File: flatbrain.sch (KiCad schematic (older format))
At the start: 101 parts, among them J1 OLED, SW1 SW_Push, U1 kbd_ProMicro

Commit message: Update mx footprints
TODO
 * verify the diode placement
 * replace right 1.75u with 1u + encoder
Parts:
- MX1, MX10, MX11, MX12, MX13, MX14, MX15, MX16, MX17, MX18, MX19, MX2, MX20, MX21, MX22, MX23, MX24, MX25, MX26, MX27, MX28, MX29, MX3, MX30, MX31, MX32, MX33, MX34, MX35, MX36, MX37, MX38, MX4, MX43, MX44, MX5, MX6, MX7, MX8, MX9: footprint MX_Only:MXOnly-1U-NoLED -> parts:mx_1u
- MX39, MX42: footprint MX_Only:MXOnly-1.75U-NoLED -> parts:mx_175u
- MX40, MX41: footprint MX_Only:MXOnly-1.5U-NoLED -> parts:mx_15u

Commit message: Correct leds connection
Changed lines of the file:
@@
 L power:GND #PWR0107
 U 1 1 5EAF3A6B
-P 1300 4650
-F 0 "#PWR0107" H 1300 4400 50  0001 C CNN
-F 1 "GND" H 1305 4477 50  0000 C CNN
-F 2 "" H 1300 4650 50  0001 C CNN
-F 3 "" H 1300 4650 50  0001 C CNN
-	1    1300 4650
-	-1   0    0    1
+P 1300 5250
+F 0 "#PWR0107" H 1300 5000 50  0001 C CNN
+F 1 "GND" H 1305 5077 50  0000 C CNN
+F 2 "" H 1300 5250 50  0001 C CNN
+F 3 "" H 1300 5250 50  0001 C CNN
+	1    1300 5250
+	1    0    0    -1
 $EndComp
 Connection ~ 1300 4650
@@
 L power:VCC #PWR0108
 U 1 1 5EAF44CC
-P 1300 5250
-F 0 "#PWR0108" H 1300 5100 50  0001 C CNN
-F 1 "VCC" H 1315 5423 50  0000 C CNN
-F 2 "" H 1300 5250 50  0001 C CNN
-F 3 "" H 1300 5250 50  0001 C CNN
-	1    1300 5250
-	-1   0    0    1
+P 1300 4650
+F 0 "#PWR0108" H 1300 4500 50  0001 C CNN
+F 1 "VCC" H 1315 4823 50  0000 C CNN
+F 2 "" H 1300 4650 50  0001 C CNN
+F 3 "" H 1300 4650 50  0001 C CNN
+	1    1300 4650
+	1    0    0    -1
 $EndComp
 Connection ~ 1300 5250

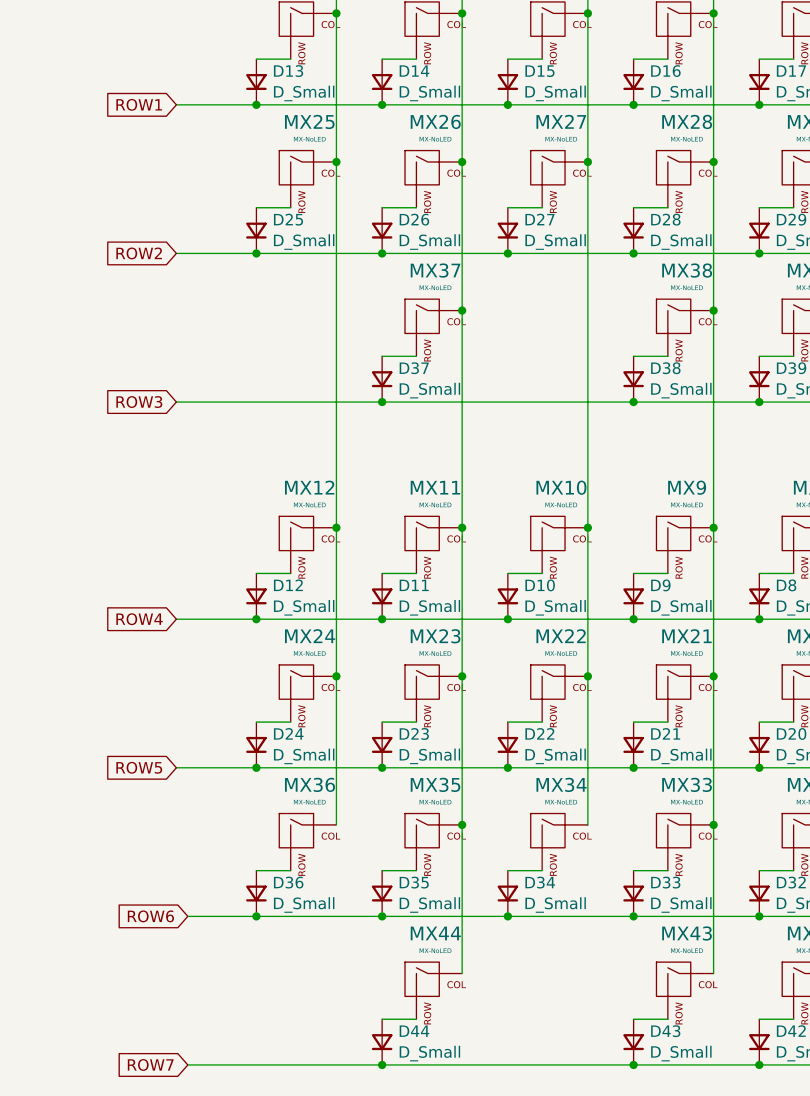
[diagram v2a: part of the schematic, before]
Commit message: Move lowest pinky keys to thumb cluster
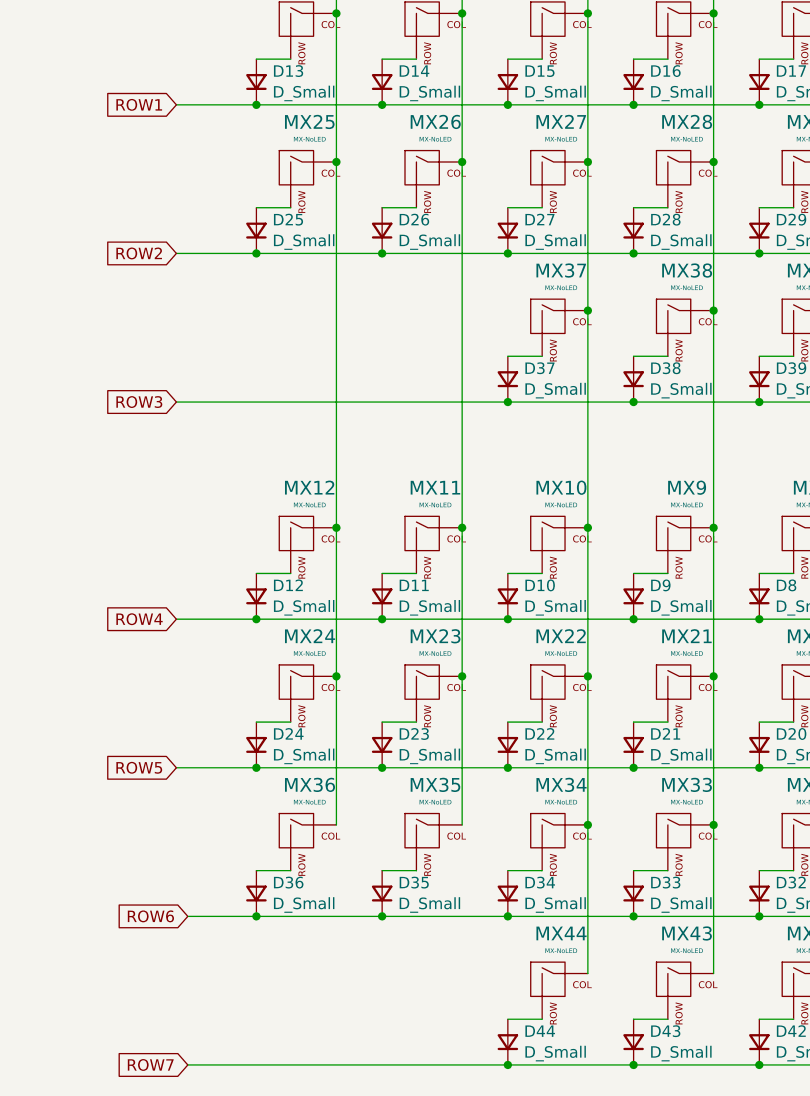
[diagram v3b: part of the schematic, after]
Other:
- moved on the sheet: D37, D44, MX37, MX44
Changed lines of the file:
@@
 	10400 1350 10250 1350
-Wire Wire Line
-	8050 3300 8200 3300
 Wire Wire Line
 	9150 3300 9300 3300
@@
 NoConn ~ 1450 2600
 Wire Wire Line
-	8400 3100 8400 2450
-Wire Wire Line
-	8050 6200 8200 6200
-Wire Wire Line
 	8400 5350 8400 4700
 Wire Wire Line
@@
 L Device:D_Small D44
 U 1 1 5EB566F4
-P 8050 6300
-F 0 "D44" V 8096 6230 50  0000 R CNN
-F 1 "D_Small" V 8005 6230 50  0000 R CNN
-F 2 "Keebio-Parts:Diode-Hybrid-Back" V 8050 6300 50  0001 C CNN
-F 3 "~" V 8050 6300 50  0001 C CNN
-	1    8050 6300
+P 8600 6300
+F 0 "D44" V 8646 6230 50  0000 R CNN
+F 1 "D_Small" V 8555 6230 50  0000 R CNN
+F 2 "Keebio-Parts:Diode-Hybrid-Back" V 8600 6300 50  0001 C CNN
+F 3 "~" V 8600 6300 50  0001 C CNN
+	1    8600 6300
 	0    -1   -1   0
 $EndComp
@@
 L MX_Alps_Hybrid:MX-NoLED MX44
 U 1 1 5EB566EE
-P 8250 6050
-F 0 "MX44" H 8283 6273 60  0000 C CNN
-F 1 "MX-NoLED" H 8283 6199 20  0000 C CNN
-F 2 "parts:mx_1u" H 7625 6025 60  0001 C CNN
-F 3 "" H 7625 6025 60  0001 C CNN
-	1    8250 6050
+P 8800 6050
+F 0 "MX44" H 8833 6273 60  0000 C CNN
+F 1 "MX-NoLED" H 8833 6199 20  0000 C CNN
+F 2 "parts:mx_1u" H 8175 6025 60  0001 C CNN
+F 3 "" H 8175 6025 60  0001 C CNN
+	1    8800 6050
 	1    0    0    -1
 $EndComp
@@
 L Device:D_Small D37
 U 1 1 5E98CCFF
-P 8050 3400
-F 0 "D37" V 8096 3330 50  0000 R CNN
-F 1 "D_Small" V 8005 3330 50  0000 R CNN
-F 2 "Keebio-Parts:Diode-Hybrid-Back" V 8050 3400 50  0001 C CNN
-F 3 "~" V 8050 3400 50  0001 C CNN
-	1    8050 3400
+P 8600 3400
+F 0 "D37" V 8646 3330 50  0000 R CNN
+F 1 "D_Small" V 8555 3330 50  0000 R CNN
+F 2 "Keebio-Parts:Diode-Hybrid-Back" V 8600 3400 50  0001 C CNN
+F 3 "~" V 8600 3400 50  0001 C CNN
+	1    8600 3400
 	0    -1   -1   0
 $EndComp
@@
 L MX_Alps_Hybrid:MX-NoLED MX37
 U 1 1 5E98CCF9
-P 8250 3150
-F 0 "MX37" H 8283 3373 60  0000 C CNN
-F 1 "MX-NoLED" H 8283 3299 20  0000 C CNN
-F 2 "parts:mx_1u" H 7625 3125 60  0001 C CNN
-F 3 "" H 7625 3125 60  0001 C CNN
-	1    8250 3150
+P 8800 3150
+F 0 "MX37" H 8833 3373 60  0000 C CNN
+F 1 "MX-NoLED" H 8833 3299 20  0000 C CNN
+F 2 "parts:mx_1u" H 8175 3125 60  0001 C CNN
+F 3 "" H 8175 3125 60  0001 C CNN
+	1    8800 3150
 	1    0    0    -1
 $EndComp
@@
 Connection ~ 9500 3100
 Wire Wire Line
-	8950 4050 8950 2450
+	8950 4050 8950 3100
 Connection ~ 8950 4050
 Connection ~ 8950 2450
-Connection ~ 8050 3500
-Wire Wire Line
-	8050 3500 9150 3500
 Connection ~ 8400 2450
-Wire Wire Line
-	7150 3500 8050 3500
-Wire Wire Line
-	8400 4050 8400 3100
 Connection ~ 8400 4050
-Connection ~ 8400 3100
 Wire Wire Line
 	7850 4050 7850 2450
@@
 Wire Wire Line
 	10250 6400 9700 6400
-Connection ~ 8050 6400
-Wire Wire Line
-	8050 6400 7200 6400
 Connection ~ 9150 6400
 Wire Wire Line
-	9150 6400 8050 6400
+	9150 6400 8600 6400
 Connection ~ 9700 6400
 Wire Wire Line
@@
 	10600 6000 10600 5350
 Connection ~ 10600 5350
-Wire Wire Line
-	8400 6000 8400 5350
-Connection ~ 8400 5350
 Wire Wire Line
 	9500 6000 9500 5350
@@
 Connection ~ 1300 5250
 NoConn ~ 1000 5950
+Connection ~ 8950 3100
+Wire Wire Line
+	8950 3100 8950 2450
+Connection ~ 8600 3500
+Wire Wire Line
+	8600 3500 9150 3500
+Wire Wire Line
+	8400 2450 8400 4050
+Wire Wire Line
+	7150 3500 8600 3500
+Wire Wire Line
+	8600 3300 8750 3300
+Connection ~ 8600 6400
+Wire Wire Line
+	7200 6400 8600 6400
+Wire Wire Line
+	8600 6200 8750 6200
+Wire Wire Line
+	8950 6000 8950 5350
+Connection ~ 8950 5350
 $EndSCHEMATC

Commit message: Work in progress:
Replace pro-micro with Elite-C
Add 2 rotary encoders
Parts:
- added D41, D42: D_Small, Keebio-Parts:Diode-Hybrid-Back, symbol Device:D_Small
- added JP1, JP2, JP3: Jumper_NO_Small, Jumper:SolderJumper-2_P1.3mm_Open_Pad1.0x1.5mm, symbol Device:Jumper_NO_Small
- added SW41, SW42: Rotary_Encoder_Switch, parts:rotary_x_mx, symbol Device:Rotary_Encoder_Switch
- J1: symbol corne-light-cache:Connector_Generic_Conn_01x04 -> flatbrain:Connector_Generic_Conn_01x04
- MX39: footprint parts:mx_175u -> parts:mx_1u
- MX40: footprint parts:mx_15u -> parts:mx_1u
- MX43: renamed from MX41; footprint parts:mx_15u -> parts:mx_1u
- MX44: renamed from MX42; footprint parts:mx_175u -> parts:mx_1u
- U1: value kbd_ProMicro -> Elite-C; footprint Keebio-Parts:ArduinoProMicro -> Keebio-Parts:Elite-C; symbol corne-light-cache:kbd_ProMicro -> flatbrain:Elite-C
- renumbered D41 to D43, D42 to D44, D43 to D45, D44 to D46, MX43 to MX45, MX44 to MX46
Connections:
- net labels added: COL10, COL11, COL6, COL7, COL8, COL9, ENC1A, ENC1B, ENC2A, ENC2B
- net labels removed: ROW4, ROW5, ROW6, ROW7
- wire segments 161 -> 168
- no-connect marks 3 -> 2
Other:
- moved on the sheet: D1, D10, D11, D12, D13, D14, D15, D16, D17, D18, D19, D2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

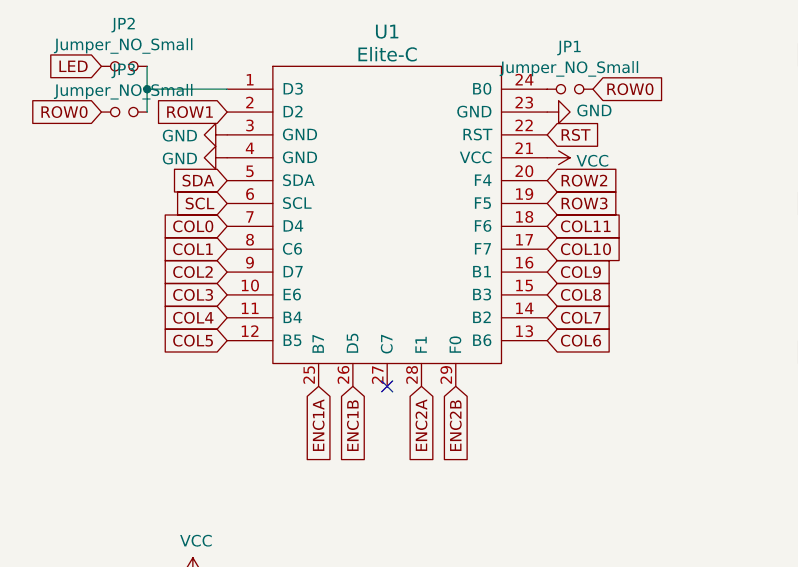
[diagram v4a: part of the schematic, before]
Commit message: Reroute left half
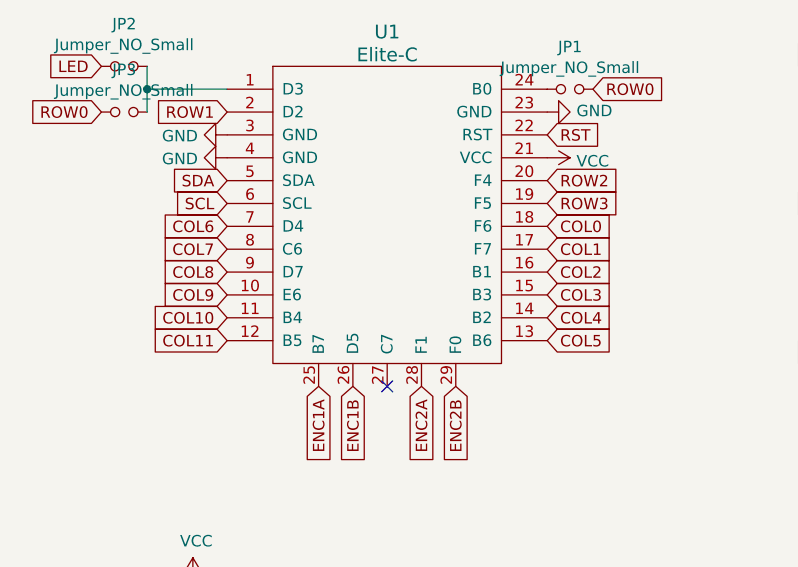
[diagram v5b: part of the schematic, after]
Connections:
- net COL0: now also U1.18 (F6); no longer U1.7 (D4)
- net COL1: now also U1.17 (F7); no longer U1.8 (C6)
- net COL10: now also U1.11 (B4); no longer U1.17 (F7)
- net COL11: now also U1.12 (B5); no longer U1.18 (F6)
- net COL2: now also U1.16 (B1); no longer U1.9 (D7)
- net COL3: now also U1.15 (B3); no longer U1.10 (E6)
- net COL4: now also U1.14 (B2); no longer U1.11 (B4)
- net COL5: now also U1.13 (B6); no longer U1.12 (B5)
- net COL6: now also U1.7 (D4); no longer U1.13 (B6)
- net COL7: now also U1.8 (C6); no longer U1.14 (B2)
- net COL8: now also U1.9 (D7); no longer U1.15 (B3)
- net COL9: now also U1.10 (E6); no longer U1.16 (B1)
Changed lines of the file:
@@
 	0    -1   -1   0
 $EndComp
-Text GLabel 1450 3100 0    50   Input ~ 0
+Text GLabel 2850 3100 2    50   Input ~ 0
 COL0
+Text GLabel 2850 3200 2    50   Input ~ 0
+COL1
+Text GLabel 2850 3300 2    50   Input ~ 0
+COL2
+Text GLabel 2850 3400 2    50   Input ~ 0
+COL3
 Text GLabel 1450 3200 0    50   Input ~ 0
-COL1
-Text GLabel 1450 3300 0    50   Input ~ 0
-COL2
-Text GLabel 1450 3400 0    50   Input ~ 0
-COL3
-Text GLabel 2850 3500 2    50   Input ~ 0
 COL7
 Text GLabel 2850 2900 2    50   Input ~ 0
@@
 Text GLabel 2850 3000 2    50   Input ~ 0
 ROW3
-Text GLabel 2850 3600 2    50   Input ~ 0
+Text GLabel 1450 3100 0    50   Input ~ 0
 COL6
 $Comp
@@
 Text GLabel 900  2600 0    50   Input ~ 0
 ROW0
+Text GLabel 2850 3500 2    50   Input ~ 0
+COL4
+Text GLabel 2850 3600 2    50   Input ~ 0
+COL5
+Text GLabel 1450 3300 0    50   Input ~ 0
+COL8
+Text GLabel 1450 3400 0    50   Input ~ 0
+COL9
 Text GLabel 1450 3500 0    50   Input ~ 0
-COL4
+COL10
 Text GLabel 1450 3600 0    50   Input ~ 0
-COL5
-Text GLabel 2850 3400 2    50   Input ~ 0
-COL8
-Text GLabel 2850 3300 2    50   Input ~ 0
-COL9
-Text GLabel 2850 3200 2    50   Input ~ 0
-COL10
-Text GLabel 2850 3100 2    50   Input ~ 0
 COL11
 Text GLabel 1450 2600 0    50   Input ~ 0

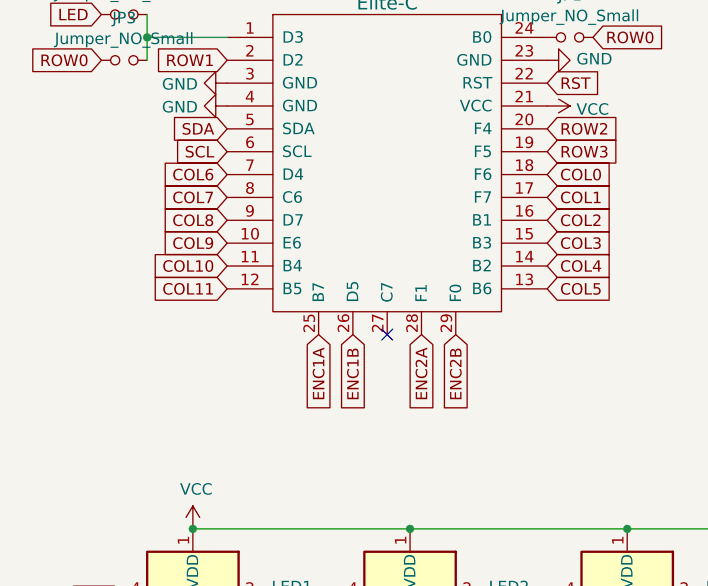
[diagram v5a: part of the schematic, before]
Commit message: The routing is over jeez
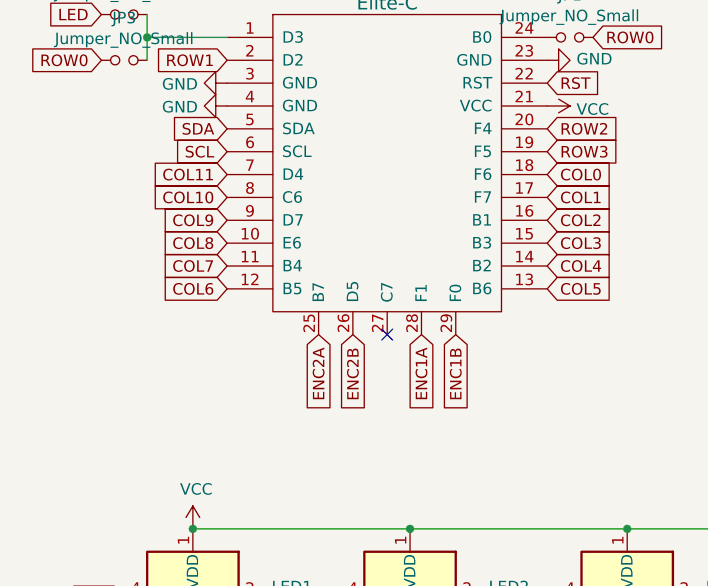
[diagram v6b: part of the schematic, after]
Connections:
- net COL10: now also U1.8 (C6); no longer U1.11 (B4)
- net COL11: now also U1.7 (D4); no longer U1.12 (B5)
- net COL6: now also U1.12 (B5); no longer U1.7 (D4)
- net COL7: now also U1.11 (B4); no longer U1.8 (C6)
- net COL8: now also U1.10 (E6); no longer U1.9 (D7)
- net COL9: now also U1.9 (D7); no longer U1.10 (E6)
- net ENC1A: now also U1.28 (F1); no longer U1.25 (B7)
- net ENC1B: now also U1.29 (F0); no longer U1.26 (D5)
- net ENC2A: now also U1.25 (B7); no longer U1.28 (F1)
- net ENC2B: now also U1.26 (D5); no longer U1.29 (F0)
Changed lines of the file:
@@
 Text GLabel 2850 3400 2    50   Input ~ 0
 COL3
-Text GLabel 1450 3200 0    50   Input ~ 0
+Text GLabel 1450 3500 0    50   Input ~ 0
 COL7
 Text GLabel 2850 2900 2    50   Input ~ 0
@@
 Text GLabel 2850 3000 2    50   Input ~ 0
 ROW3
-Text GLabel 1450 3100 0    50   Input ~ 0
+Text GLabel 1450 3600 0    50   Input ~ 0
 COL6
 $Comp
@@
 Text GLabel 2850 3600 2    50   Input ~ 0
 COL5
+Text GLabel 1450 3400 0    50   Input ~ 0
+COL8
 Text GLabel 1450 3300 0    50   Input ~ 0
-COL8
-Text GLabel 1450 3400 0    50   Input ~ 0
 COL9
-Text GLabel 1450 3500 0    50   Input ~ 0
+Text GLabel 1450 3200 0    50   Input ~ 0
 COL10
-Text GLabel 1450 3600 0    50   Input ~ 0
+Text GLabel 1450 3100 0    50   Input ~ 0
 COL11
 Text GLabel 1450 2600 0    50   Input ~ 0
 ROW1
-Text GLabel 1850 3800 3    50   Input ~ 0
+Text GLabel 2300 3800 3    50   Input ~ 0
 ENC1A
-Text GLabel 2000 3800 3    50   Input ~ 0
+Text GLabel 2450 3800 3    50   Input ~ 0
 ENC1B
-Text GLabel 2300 3800 3    50   Input ~ 0
-ENC2A
-Text GLabel 2450 3800 3    50   Input ~ 0
-ENC2B
 Text GLabel 3050 2500 2    50   Input ~ 0
 ROW0
 NoConn ~ 2150 3800
+Text GLabel 2000 3800 3    50   Input ~ 0
+ENC2B
+Text GLabel 1850 3800 3    50   Input ~ 0
+ENC2A
 $EndSCHEMATC

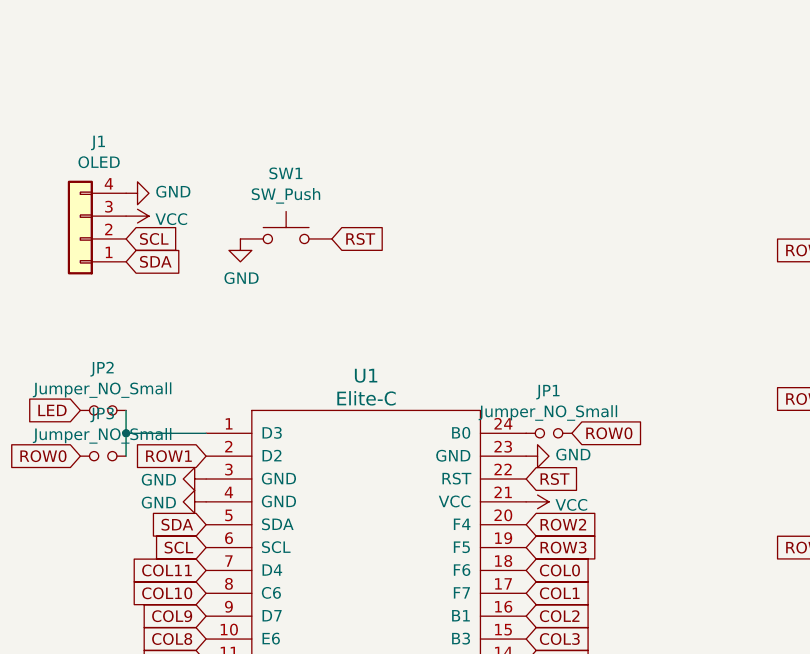
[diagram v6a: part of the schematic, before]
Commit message: Remove gerber file
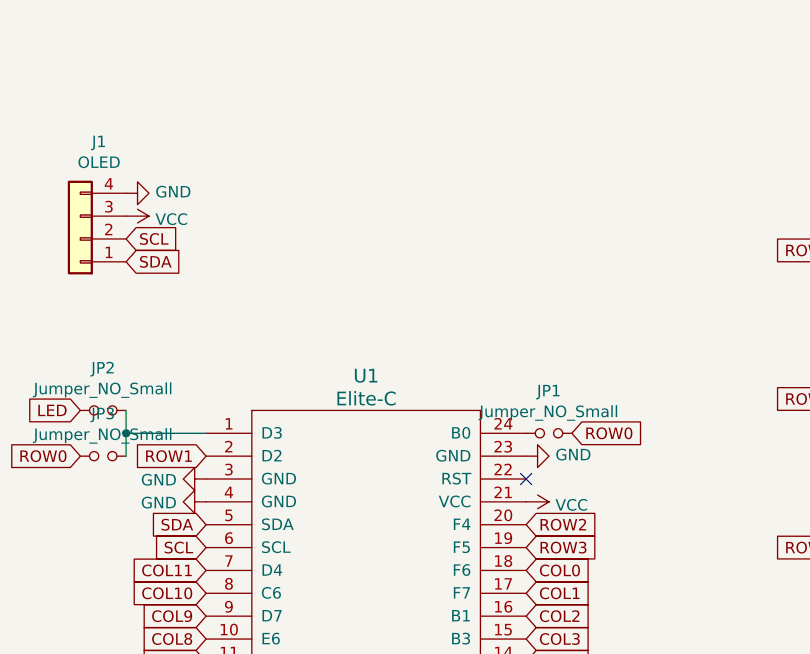
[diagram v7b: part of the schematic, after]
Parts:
- removed SW1: SW_Push, random-keyboard-parts:SKQG-1155865, symbol Switch:SW_Push
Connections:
- net RST: no longer names the net of U1.22 (RST)
- no-connect marks 2 -> 3
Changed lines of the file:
@@
 Comment4 ""
 $EndDescr
-$Comp
-L power:GND #PWR0109
-U 1 1 5E8A23B9
-P 1600 1650
-F 0 "#PWR0109" H 1600 1400 50  0001 C CNN
-F 1 "GND" H 1605 1477 50  0000 C CNN
-F 2 "" H 1600 1650 50  0001 C CNN
-F 3 "" H 1600 1650 50  0001 C CNN
-	1    1600 1650
-	1    0    0    -1
-$EndComp
 Wire Wire Line
 	4600 1500 4750 1500
@@
 Wire Wire Line
 	9350 1950 9350 1300
-Text GLabel 2000 1650 2    50   Input ~ 0
-RST
-Text GLabel 2850 2700 2    50   Input ~ 0
-RST
 $Comp
 L power:GND #PWR0101
@@
 F 3 "" H 4175 1325 60  0001 C CNN
 	1    4800 1350
-	1    0    0    -1
-$EndComp
-$Comp
-L Switch:SW_Push SW1
-U 1 1 5E8A1EA9
-P 1800 1650
-F 0 "SW1" H 1800 1935 50  0000 C CNN
-F 1 "SW_Push" H 1800 1844 50  0000 C CNN
-F 2 "random-keyboard-parts:SKQG-1155865" H 1800 1850 50  0001 C CNN
-F 3 "~" H 1800 1850 50  0001 C CNN
-	1    1800 1650
 	1    0    0    -1
 $EndComp
@@
 Text GLabel 1850 3800 3    50   Input ~ 0
 ENC2A
+NoConn ~ 2850 2700
 $EndSCHEMATC

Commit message: Add choc support
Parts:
- MX1, MX10, MX11, MX12, MX13, MX14, MX15, MX16, MX17, MX18, MX19, MX2, MX20, MX21, MX22, MX23, MX24, MX25, MX26, MX27, MX28, MX29, MX3, MX30, MX31, MX32, MX33, MX34, MX35, MX36, MX37, MX38, MX39, MX4, MX40, MX43, MX44, MX45, MX46, MX5, MX6, MX7, MX8, MX9: footprint parts:mx_1u -> parts:mxchoc_1u
- SW41, SW42: footprint parts:rotary_x_mx -> parts:rotary_x_mxchoc
